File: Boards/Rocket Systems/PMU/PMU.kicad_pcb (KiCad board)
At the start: 2 copper layers, 131 parts, among them IC1 LM4040DIZ-4.1_NOPB, IC2 LM4040DIZ-4.1_NOPB, IC3 LM4040DIZ-4.1_NOPB, IC4 LS1205EFD33, J2 XT30UPB-F, J3 XT30UPB-F, J4 XT30UPB-F, J5 XT30UPB-F, K3 G3VM-31DR_TR05_, K4 G3VM-31DR_TR05_, K5 G3VM-31DR_TR05_, Q1 NPN, Q2 PMOS, Q3 NPN, Q4 NPN, Q5 NPN, Q6 NPN, Q7 NPN, Q8 NPN, U10 ST1L05APU33R, U29 NCV8114ASN165T1G, U3 STPS15L45CB, U30 MCP6002-E/MS, U4 STPS15L45CB, U7 NJD35N04T4G, U8 NJD35N04T4G, U9 NJD35N04T4G

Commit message: PMU BROW BROW
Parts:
- moved CR8 188.4 mm to (202.8, 67.0), turned to 180 degrees
- moved CR7 182.4 mm to (197.5, 67.0)
- moved R27 174.1 mm to (205.8, 62.1), turned to 90 degrees
- moved Q5 172.3 mm to (191.8, 74.7), turned to 90 degrees
- moved R18 171.9 mm to (194.5, 62.1), turned to 90 degrees
- moved CR6 169.1 mm to (181.2, 57.8)
- moved R21 168.1 mm to (192.9, 110.8)
- moved CR4 165.9 mm to (182.2, 67.8)
- moved CR9 165.6 mm to (185.5, 94.0), turned to 180 degrees
- moved Q4 164.5 mm to (186.2, 82.8), turned to -90 degrees
- moved Q6 164.3 mm to (191.8, 82.1)
- moved CR10 162.5 mm to (181.8, 94.0)
- moved R28 160.8 mm to (190.8, 95.0)
- moved Q8 159.6 mm to (184.5, 74.0), turned to 90 degrees
- moved R17 159.4 mm to (181.0, 53.1), turned to 90 degrees
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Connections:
- R37 pad 1: /V1_OUT -> /V5_OUT
- R40 pad 1: /V4_OUT -> /V1_OUT
- R41 pad 1: /V5_OUT -> /V4_OUT
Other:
- board outline added: 77.5 x 88.8 mm
- copper layers 2 -> 4
- board text added: "shoot"

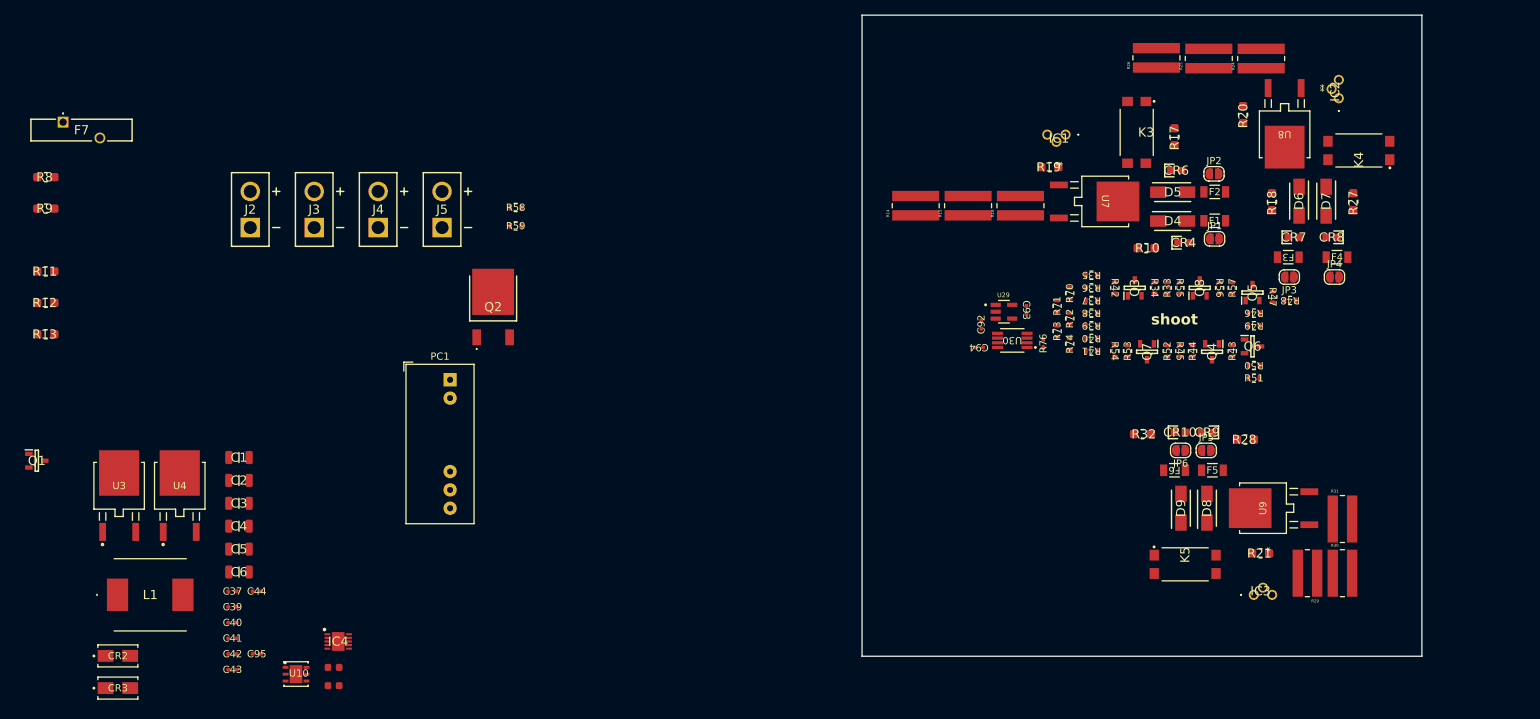
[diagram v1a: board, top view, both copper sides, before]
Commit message: PMU layout
Full layout
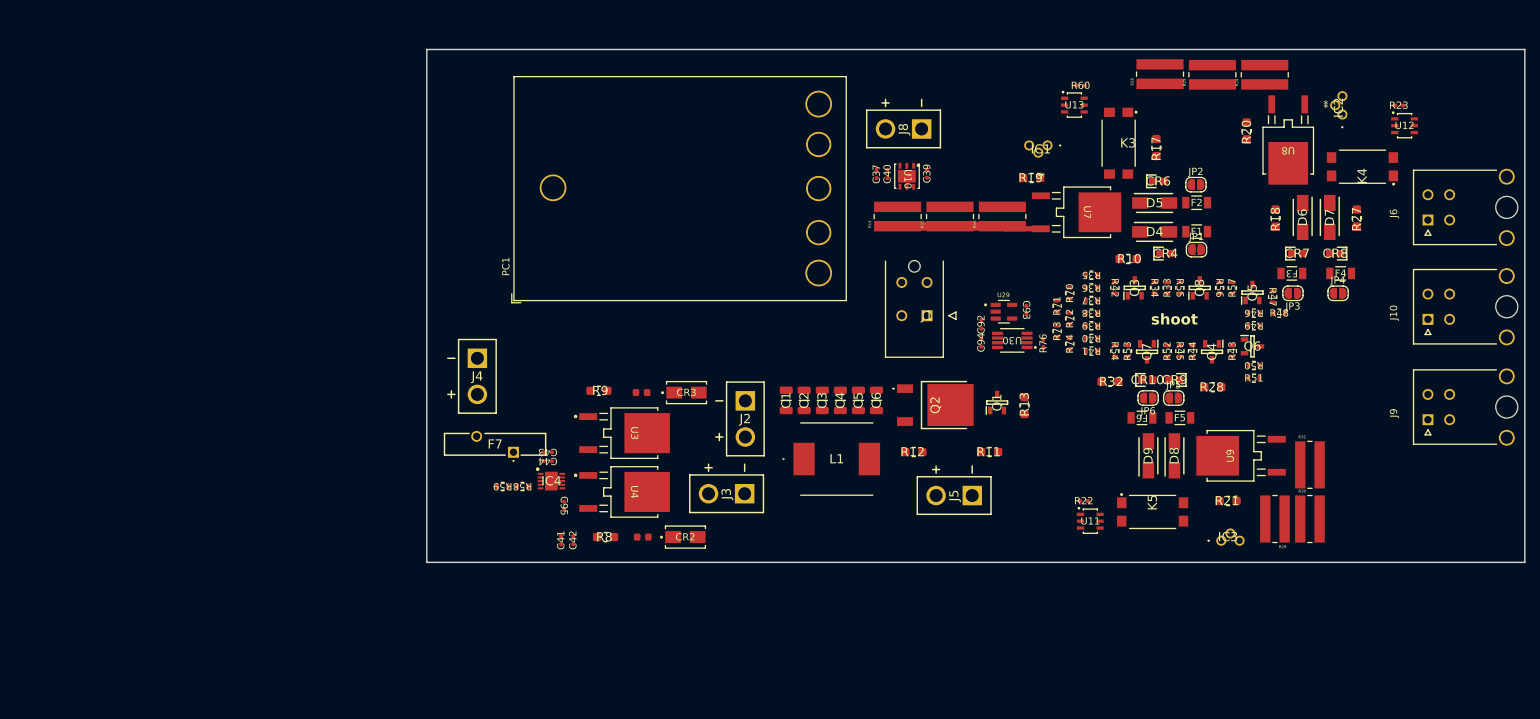
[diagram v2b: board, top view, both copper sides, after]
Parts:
- added J1: 172298-1104, 1722981104:172298-YY04, F.Cu at (146.8, 77.8)
- added J10: 1723163304, 1723163304:MOLEX_1723163304, F.Cu at (216.1, 78.4)
- added J6: 1723163304, 1723163304:MOLEX_1723163304, F.Cu at (216.1, 64.6)
- added J8: XT30UPB-F, XT30UPB-F:XT30UPBF, F.Cu at (146.0, 52.0)
- added J9: 1723163304, 1723163304:MOLEX_1723163304, F.Cu at (216.1, 92.2)
- added R22: 10k, Resistor-0402:RES_0402, F.Cu at (168.4, 103.5)
- added R23: 10k, Resistor-0402:RES_0402, F.Cu at (212.1, 48.8)
- added R60: 10k, Resistor-0402:RES_0402, F.Cu at (168.0, 46.0)
- added U11: NCR321UX, LED Driver_NCR321UX:TSOP6_SOT457_NEX, F.Cu at (169.4, 106.3)
- added U12: NCR321UX, LED Driver_NCR321UX:TSOP6_SOT457_NEX, F.Cu at (212.9, 51.5)
- added U13: NCR321UX, LED Driver_NCR321UX:TSOP6_SOT457_NEX, F.Cu at (167.1, 48.7)
- moved R13 135.8 mm to (160.2, 90.3), turned to -90 degrees
- moved Q1 133.2 mm to (156.4, 89.9), turned to 90 degrees
- moved R11 133.0 mm to (155.4, 96.7)
- moved R12 121.9 mm to (144.9, 96.7)
- moved C39 113.3 mm to (146.8, 58.2), turned to 90 degrees
- moved C40 109.9 mm to (141.2, 58.2), turned to 90 degrees
- moved U10 109.1 mm to (144.0, 58.6), turned to -90 degrees
- moved C37 106.2 mm to (139.8, 58.2), turned to 90 degrees
- moved L1 96.9 mm to (134.2, 97.7)
- moved R8 92.1 mm to (102.2, 108.5)
- moved C6 91.4 mm to (139.8, 89.6), turned to 90 degrees
- moved CR3 88.7 mm to (113.5, 88.5)
- moved C5 88.2 mm to (137.2, 89.6), turned to 90 degrees
- moved C4 85.1 mm to (134.8, 89.6), turned to 90 degrees
- moved J5 82.2 mm to (153.0, 102.8), turned to 90 degrees
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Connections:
- IC4 pad 5: Net-(IC4-ILIM) -> unconnected-(IC4-ILIM-Pad5)
- R58 pad 1: Net-(IC4-ILIM) -> unconnected-(R58-Pad1)
- R59 pad 2: GND -> unconnected-(R59-Pad2)
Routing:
- net Net-(U7-E): track 0.00 -> 20.0 mm
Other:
- board size 77.5 x 88.8 mm -> 152 x 71 mm

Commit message: PMU
basicamente feito
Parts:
- added H2: MountingHole, MountingHole:MountingHole_3.2mm_M3_ISO7380, F.Cu at (82.5, 46.0)
- added H2: MountingHole, MountingHole:MountingHole_3.2mm_M3_ISO7380, F.Cu at (224.5, 107.0)
- added H2: MountingHole, MountingHole:MountingHole_3.2mm_M3_ISO7380, F.Cu at (224.5, 46.0)
- added H2: MountingHole, MountingHole:MountingHole_3.2mm_M3_ISO7380, F.Cu at (82.5, 107.0)
- moved R14 21.5 mm to (163.2, 70.4), turned to -90 degrees
- moved J5 12.5 mm to (152.0, 90.3)
- moved Q2 11.5 mm to (152.0, 101.0), turned to 180 degrees
- moved R15 8.74 mm to (156.0, 70.4), turned to -90 degrees
- moved Q1 7.35 mm to (159.3, 96.7), turned to 180 degrees
- moved R11 7.05 mm to (159.2, 90.8)
- moved R13 6.06 mm to (163.8, 95.2)
- moved R60 4.83 mm to (163.5, 47.8), turned to 180 degrees
- moved R22 3.47 mm to (165.4, 105.2), turned to 180 degrees
- moved R12 3.38 mm to (144.5, 100.1), turned to -90 degrees
- moved C94 3.13 mm to (156.5, 83.8), turned to 0 degrees
- moved CR10 2.25 mm to (175.0, 86.8)
- moved R32 2.25 mm to (169.8, 87.0)
- moved D9 1.89 mm to (175.5, 97.2)
- moved C92 1.82 mm to (153.8, 77.3), turned to 180 degrees
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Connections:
- IC4 pad 5: unconnected-(IC4-ILIM-Pad5) -> Net-(IC4-ILIM)
- J1 pad 2: /RECOVERY2 -> /RECOVERY3
- J1 pad 3: /RECOVERY3 -> /RECOVERY2
- R58 pad 1: unconnected-(R58-Pad1) -> Net-(IC4-ILIM)
- R59 pad 2: unconnected-(R59-Pad2) -> GND
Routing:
- net +3.3V: track 0.00 -> 192.6 mm, vias 0 -> 19
- net +5V: track 0.00 -> 187.0 mm, vias 0 -> 17
- net /RECOVERY2: track 0.00 -> 79.7 mm, vias 0 -> 4
- net GND: track 0.00 -> 58.5 mm, vias 0 -> 4
- net VDC: track 0.00 -> 50.9 mm
- net /RECOVERY3: track 0.00 -> 44.6 mm, vias 0 -> 2
- net /PYRO6_OUT: track 0.00 -> 37.1 mm, vias 0 -> 3
- net /RECOVERY1: track 0.00 -> 36.2 mm
- net /PYRO5_OUT: track 0.00 -> 30.7 mm
- net /PYRO1_OUT: track 0.00 -> 29.3 mm, vias 0 -> 3
- net /PYRO2_OUT: track 0.00 -> 28.2 mm, vias 0 -> 3
- net /V3_IN: track 0.00 -> 24.4 mm
- net VBAT1: track 0.00 -> 23.4 mm
- net /V2_OUT: track 0.00 -> 22.0 mm
- net /V1_OUT: track 0.00 -> 20.5 mm
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- added copper zone on B.Cu, net +3.3V
- added copper zone on F.Cu, net +3.3V
- added copper zone on F.Cu, net +5V
- added copper zone on F.Cu, net /I_ENABLE
- added copper zone on F.Cu, net /PYRO1_OUT
- added copper zone on F.Cu, net /PYRO2_OUT
- added copper zone on F.Cu, net /PYRO3_OUT
- added copper zone on F.Cu, net /PYRO4_OUT
- added copper zone on F.Cu, net /PYRO5_OUT
- added copper zone on F.Cu, net /PYRO6_OUT
- added copper zone on F.Cu, net /RECOVERY2
- added copper zone on F.Cu, net /RECOVERY3
- added copper zone on F.Cu, net /V0_IN
- added copper zone on F.Cu, net /V2_OUT
- added copper zone on F.Cu, net /V3_OUT
- added copper zone on F.Cu, net /V5_IN
- added copper zone on F.Cu, net GND
- added copper zone on In1.Cu, net GND
- added copper zone on In2.Cu, net GND
- added copper zone on F.Cu, net Net-(IC4-OUT_1)
- added copper zone on F.Cu, net Net-(U7-E)
- added copper zone on F.Cu, net Net-(U8-E)
- added copper zone on F.Cu, net Net-(U9-E)
- added copper zone on F.Cu, net VBAT1
- added copper zone on F.Cu, net VDC
- added copper zone on B.Cu, net VParachute
- added copper zone on F.Cu, net VParachute
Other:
- board text added: "5V"
- board text added: "BAT1"
- board text added: "BAT2"
- board text added: "CORTEX"
- board text added: "Eagle 1"
- board text added: "Eagle 2"
- board text added: "Filling Station"
- board text added: "JOY-IT SBC-Buck02 5V"
- board text added: "Tender Descender"

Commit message: PMU banger
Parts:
- removed the H2 at (82.5, 46.0)
- removed the H2 at (224.5, 107.0)
- removed the H2 at (224.5, 46.0)
- removed the H2 at (82.5, 107.0)
- added 1V65: TestPoint, TestPoint:TestPoint_Pad_2.0x2.0mm, F.Cu at (161.1, 74.3)
- added 3V3: TestPoint, TestPoint:TestPoint_Pad_2.0x2.0mm, F.Cu at (149.6, 58.2)
- added 5V: TestPoint, TestPoint:TestPoint_Pad_2.0x2.0mm, F.Cu at (140.6, 46.9)
- added GND: TestPoint, TestPoint:TestPoint_Pad_2.0x2.0mm, F.Cu at (225.1, 101.6)
- added H1: MountingHole, MountingHole:MountingHole_3.2mm_M3_ISO7380, F.Cu at (194.6, 89.8)
- added H2: MountingHole, MountingHole:MountingHole_3.2mm_M3_ISO7380, F.Cu at (194.6, 62.8)
- added H3: MountingHole, MountingHole:MountingHole_3.2mm_M3_ISO7380, F.Cu at (134.6, 89.8)
- added VBAT1: TestPoint, TestPoint:TestPoint_Pad_2.0x2.0mm, F.Cu at (126.3, 80.7)
- added VBAT2: TestPoint, TestPoint:TestPoint_Pad_2.0x2.0mm, F.Cu at (121.2, 105.3)
- added VParachute: TestPoint, TestPoint:TestPoint_Pad_2.0x2.0mm, F.Cu at (218.7, 101.6)
- moved R26 48.7 mm to (225.8, 50.8), turned to -90 degrees
- moved R25 34.3 mm to (218.5, 50.8), turned to -90 degrees
- moved J4 25.3 mm to (109.8, 81.6), turned to 90 degrees
- moved R24 20.2 mm to (211.2, 50.8), turned to -90 degrees
- moved C41 19.8 mm to (102.2, 89.5), turned to -90 degrees
- moved C42 19.3 mm to (100.9, 89.5), turned to -90 degrees
- moved IC2 18.0 mm to (188.0, 57.8), turned to 0 degrees
- moved R29 14.2 mm to (208.6, 102.0), turned to -90 degrees
- moved IC3 13.7 mm to (199.9, 103.2)
- moved R30 12.5 mm to (208.6, 97.1), turned to 90 degrees
- moved F7 11.1 mm to (96.2, 88.0), turned to 90 degrees
- moved C9 10.8 mm to (117.9, 87.0)
- moved U3 10.7 mm to (116.7, 92.3)
- moved J5 9.93 mm to (161.5, 87.3)
- moved C3 9.16 mm to (141.4, 90.0)
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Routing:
- net GND: track 58.5 -> 90.5 mm, vias 4 -> 148
- net Net-(U8-E): track 16.6 -> 33.2 mm
- net Net-(IC4-OUT_1): track 4.27 -> 19.4 mm
- net +3.3V: track 192.6 -> 182.9 mm, vias 19 -> 23
- net VParachute: track 0.00 -> 9.51 mm
- net Net-(U9-E): track 4.88 -> 13.2 mm
- net Net-(C9-Pad1): track 4.05 -> 10.3 mm
- net /RECOVERY3: track 44.6 -> 39.1 mm
- net Net-(C8-Pad2): track 3.30 -> 8.30 mm
- net /RECOVERY2: track 79.7 -> 74.7 mm
- net /FIRE_OUT2: track 7.20 -> 11.8 mm
- net VBAT2: track 18.0 -> 21.9 mm
- net /PYRO6_OUT: track 37.1 -> 40.6 mm
- net Net-(U8-C): track 6.33 -> 8.95 mm
- net +1.65V: track 8.35 -> 10.8 mm
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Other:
- board size 152 x 71 mm -> 138 x 62 mm
- board text added: "Charging"
- board text added: "KEY"
- board text removed: "Filling Station"

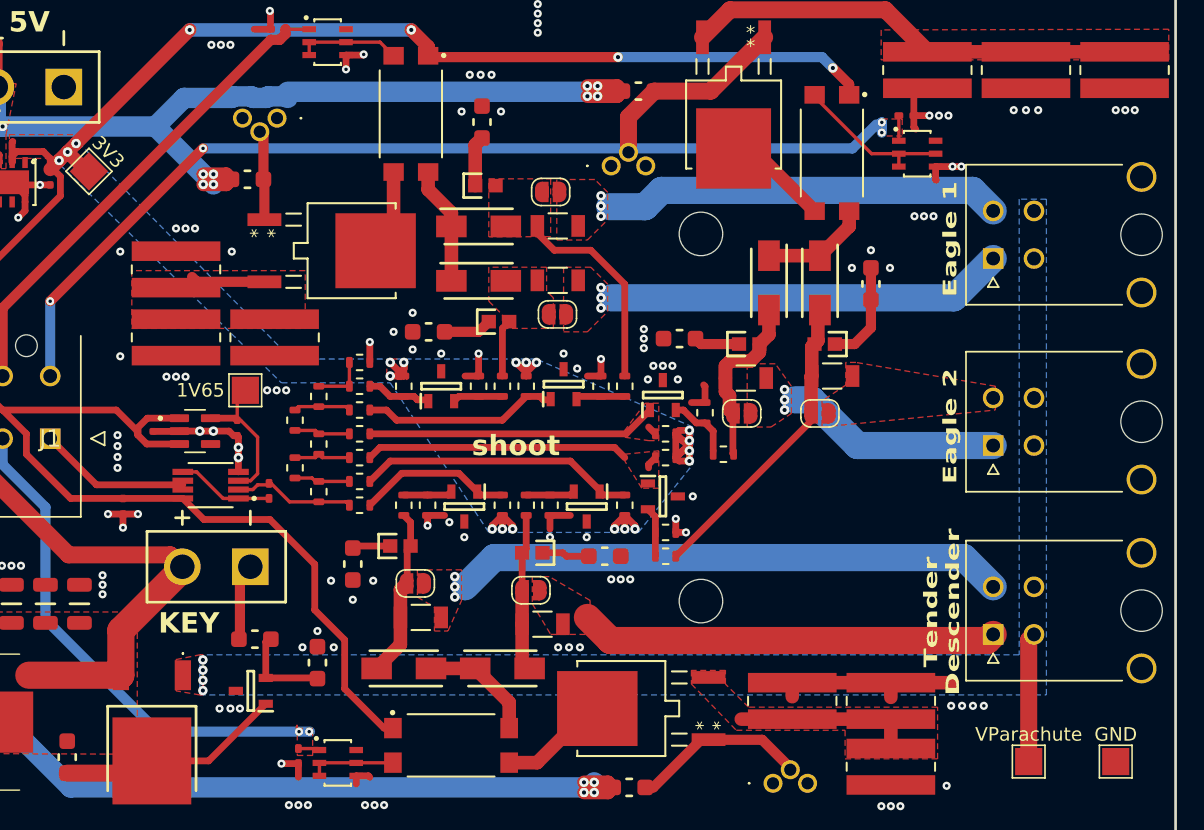
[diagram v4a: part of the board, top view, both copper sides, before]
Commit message: PMU
adição de buffers
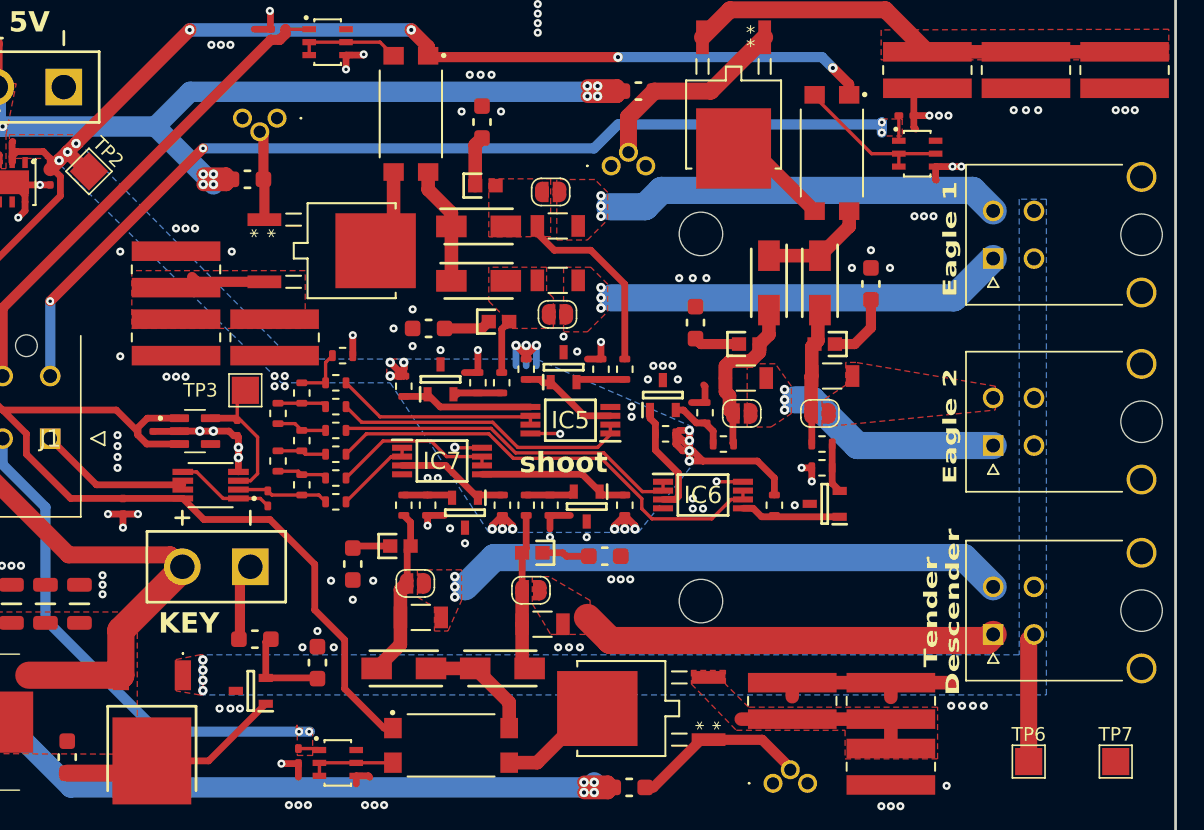
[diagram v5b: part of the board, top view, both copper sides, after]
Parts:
- added IC5: LM358BIPWR, LM358BIPWR:SOP65P640X120-8N, F.Cu at (185.0, 76.5)
- added IC6: LM358BIPWR, LM358BIPWR:SOP65P640X120-8N, F.Cu at (194.8, 82.0)
- added IC7: LM358BIPWR, LM358BIPWR:SOP65P640X120-8N, F.Cu at (175.6, 79.5)
- moved R51 14.2 mm to (203.5, 78.2), turned to 180 degrees
- moved R50 12.4 mm to (203.5, 80.0), turned to 0 degrees
- moved Q6 11.9 mm to (203.7, 82.7), turned to 180 degrees
- moved R49 8.73 mm to (200.0, 82.8), turned to -90 degrees
- moved R36 1.77 mm to (167.8, 73.8)
- moved R37 1.77 mm to (167.8, 75.5)
- moved R38 1.77 mm to (167.8, 77.2)
- moved R39 1.77 mm to (167.8, 79.0)
- moved R40 1.77 mm to (167.8, 80.8)
- moved R41 1.77 mm to (167.8, 82.5)
- moved R18 1.66 mm to (194.2, 69.3), turned to 90 degrees
- moved R35 1.35 mm to (168.2, 71.8)
- moved R71 1.35 mm to (163.5, 76.0)
- moved R73 1.35 mm to (163.5, 79.5)
- moved R74 1.35 mm to (165.2, 81.2)
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- renumbered 5V to TP1, 3V3 to TP2, 1V65 to TP3, VBAT1 to TP4, VBAT2 to TP5, VParachute to TP6, GND to TP7
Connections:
- Q3 pad 1: /V0_OUT -> /V0_BUFF
- Q4 pad 1: /V1_OUT -> /V1_BUFF
- Q5 pad 1: /V2_OUT -> /V2_BUFF
- Q6 pad 1: /V3_OUT -> /V3_BUFF
- Q7 pad 1: /V4_OUT -> /V4_BUFF
- Q8 pad 1: /V5_OUT -> /V5_BUFF
- R42 pad 2: /V0_OUT -> /V0_BUFF
- R43 pad 2: /V1_OUT -> /V1_BUFF
- R46 pad 2: /V2_OUT -> /V2_BUFF
- R49 pad 2: /V3_OUT -> /V3_BUFF
- R52 pad 2: /V4_OUT -> /V4_BUFF
- R55 pad 2: /V5_OUT -> /V5_BUFF
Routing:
- net VDC: track 51.7 -> 104.9 mm, vias 0 -> 3
- net /V3_OUT: track 20.3 -> 34.1 mm
- net /V3_IN: track 22.0 -> 10.1 mm
- net /V1_BUFF: track 0.00 -> 11.2 mm
- net /V0_OUT: track 4.76 -> 15.3 mm
- net +3.3V: track 182.9 -> 193.2 mm
- net /V0_BUFF: track 0.00 -> 10.1 mm
- net /V2_BUFF: track 0.00 -> 8.45 mm
- net /V1_OUT: track 20.5 -> 12.3 mm
- net /V4_BUFF: track 0.00 -> 8.16 mm
- net /V3_BUFF: track 0.00 -> 7.37 mm
- net /V5_BUFF: track 0.00 -> 7.36 mm
- net /V5_OUT: track 14.5 -> 21.8 mm
- net /V4_OUT: track 11.4 -> 6.15 mm
- net /V2_OUT: track 22.0 -> 26.0 mm
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- removed copper zone on F.Cu, net /V2_OUT
- removed copper zone on F.Cu, net /V3_OUT
